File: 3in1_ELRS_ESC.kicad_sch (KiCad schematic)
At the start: 32 parts, among them J1 XT30, P1 SM08B-SRSS-TB(LF)(SN), U5 LMR51420YDDCR, U6 TLV76733DRVR, U7 INA186A3IDCKR

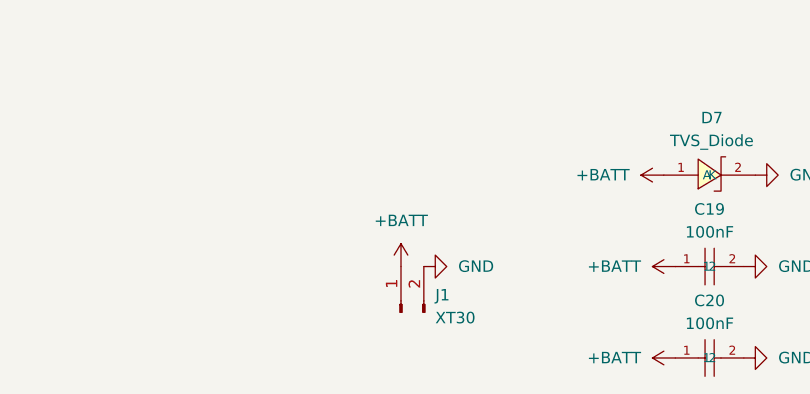
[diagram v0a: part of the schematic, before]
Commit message: FET's Placed
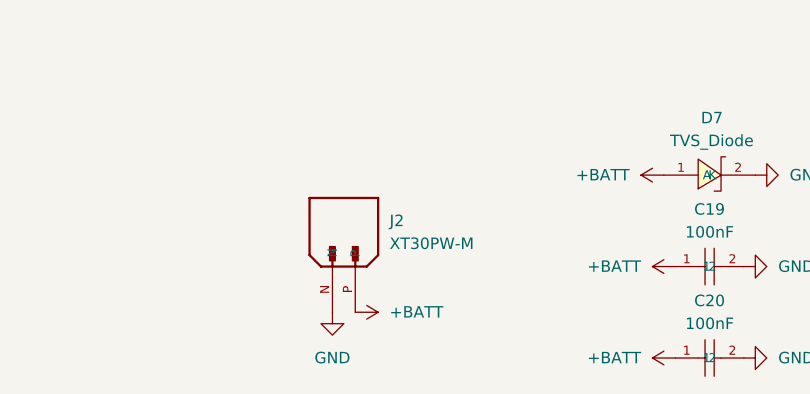
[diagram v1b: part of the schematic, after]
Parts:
- removed J1: XT30, symbol Connector:Conn_01x02_Pin
- added J2: XT30PW-M, XT30PW-M:AMASS_XT30PW-M, symbol XT30PW-M:XT30PW-M
- A1, A2, B1, B2, C1, C2, M1, M2, SWCLK_1, SWCLK_2, SWDIO_1, SWDIO_2: footprint (none) -> TestPoint:TestPoint_THTPad_2.5x2.5mm_Drill1.2mm
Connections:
- net +BATT: now also J2.P
- net GND: now also J2.N
